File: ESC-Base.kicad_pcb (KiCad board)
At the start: 2 copper layers, 32 x 51.8 mm, 35 parts, among them P1 CONN_01X03, P2 CONN_01X05, P3 CONN_01X05, P4 CONN_01X02, P5 CONN_01X02, P6 CONN_01X04, P7 CONN_01X04, P8 CONN_01X02, U1 LM1084IS-5.0/NOPB, U2 VND5E006ASPTR, U3 LTV-817, U4 ACS712_30A, U5 ACS712_30A, U6 LTV-817, U7 LTV-817

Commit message: Weiter gearbeitet...
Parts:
- C4, D1, R1, R3, R5, R6, R7, R9, U1: moved to B.Cu
- U3: footprint sven:LTV817-Footprint -> toni:SO-4
- U6, U7: footprint sven:LTV817-Footprint -> toni:SO-4; moved to B.Cu
- moved C4 126.5 mm to (59.8, 90.0), turned to 180 degrees
- moved R8 123.7 mm to (57.0, 119.0), turned to 90 degrees
- moved R7 115.9 mm to (55.4, 106.4), turned to 90 degrees
- moved R10 112.9 mm to (71.9, 119.3), turned to 90 degrees
- moved C3 108.1 mm to (48.5, 102.4), turned to 180 degrees
- moved C1 104.9 mm to (48.5, 99.5), turned to 180 degrees
- moved R9 104.4 mm to (73.7, 104.4), turned to 90 degrees
- moved R1 100.1 mm to (58.6, 92.2)
- moved C2 94.7 mm to (48.5, 97.3), turned to 180 degrees
- moved U7 92.3 mm to (73.4, 111.4), turned to 0 degrees
- moved C8 89.9 mm to (58.8, 111.6), turned to 90 degrees
- moved R3 87.9 mm to (66.3, 91.2), turned to 270 degrees
- moved C6 87.7 mm to (61.0, 109.8), turned to 90 degrees
- moved R6 85.3 mm to (68.6, 91.2), turned to 270 degrees
- moved R5 77.2 mm to (70.3, 91.2), turned to 270 degrees
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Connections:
- R7 pad 2: Net-(P4-Pad2) -> /OUT2
- R9 pad 2: Net-(P5-Pad2) -> /OUT1
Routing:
- net GND: track 0.00 -> 210.4 mm, vias 0 -> 2
- net /OUT2: track 0.00 -> 56.3 mm, vias 0 -> 20
- net VCC: track 0.00 -> 39.2 mm, vias 0 -> 10
- net /OUT1: track 0.00 -> 38.5 mm, vias 0 -> 13
- net +5V: track 3.27 -> 31.9 mm, vias 0 -> 2
- net /Vcheck2: track 0.00 -> 27.1 mm, vias 0 -> 1
- net /Vcheck1: track 0.00 -> 25.2 mm, vias 0 -> 1
- net Net-(P3-Pad3): track 0.00 -> 24.5 mm, vias 0 -> 2
- net /GNDcheck2: track 0.00 -> 21.6 mm
- net /GNDcheck1: track 0.00 -> 19.7 mm
- net Net-(P2-Pad3): track 0.00 -> 19.2 mm
- net Net-(P4-Pad2): track 0.00 -> 16.1 mm
- net Net-(P3-Pad5): track 0.00 -> 13.2 mm, vias 0 -> 1
- net Net-(C1-Pad1): track 0.00 -> 12.0 mm, vias 0 -> 1
- net Net-(P2-Pad5): track 0.00 -> 11.8 mm, vias 0 -> 1
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- added copper zone on B.Cu, net /OUT1
- added copper zone on F.Cu, net /OUT1
- added copper zone on B.Cu, net /OUT2
- added copper zone on F.Cu, net /OUT2
- added copper zone on F.Cu, net GND
- added copper zone on F.Cu, net Net-(P4-Pad2)
- added copper zone on F.Cu, net Net-(P5-Pad2)
- added copper zone on B.Cu, net VCC
- added copper zone on F.Cu, net VCC
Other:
- net class 5V added: clearance 0.4, trace_width 0.25, via_dia 0.6, via_drill 0.4

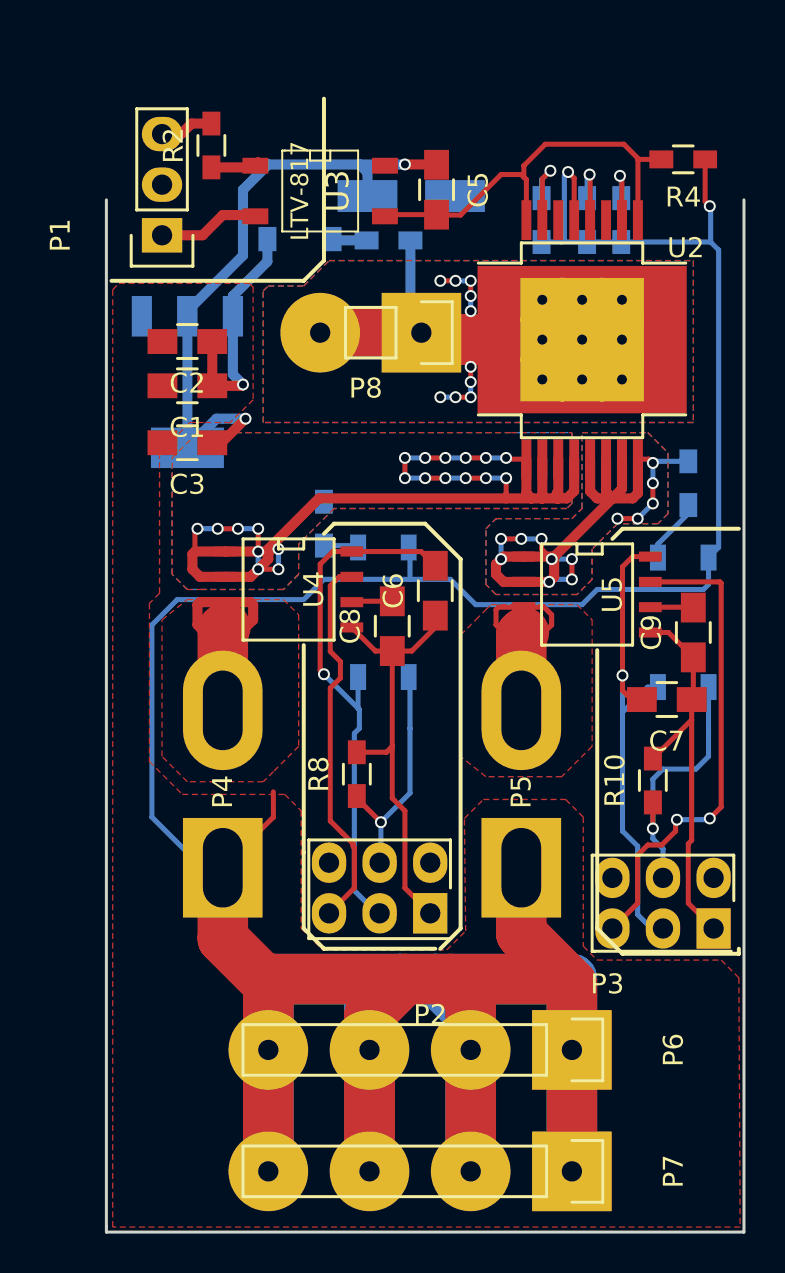
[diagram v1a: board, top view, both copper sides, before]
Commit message: Kleinere Optimierung+Netlist-Fix
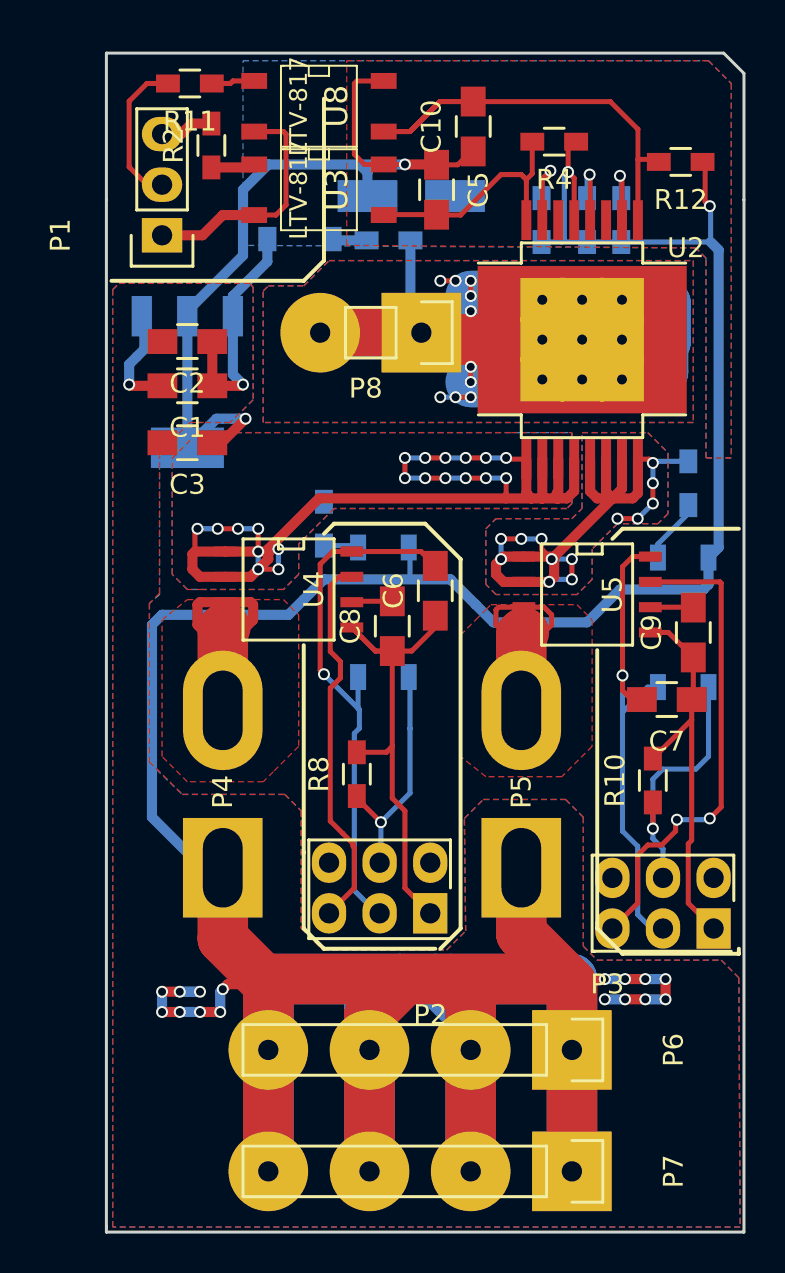
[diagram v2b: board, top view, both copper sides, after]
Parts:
- added C10: 100n, Capacitors_SMD:C_0805_HandSoldering, F.Cu at (62.9, 86.5)
- added R11: 1k, Resistors_SMD:R_0603_HandSoldering, F.Cu at (48.6, 84.3)
- added R12: 10k, Resistors_SMD:R_0603_HandSoldering, F.Cu at (73.3, 88.3)
- added U8: LTV-817, toni:SO-4, F.Cu at (55.1, 85.5)
- moved R4 6.54 mm to (66.9, 87.2)
- moved U3 0.09 mm to (55.1, 89.7)
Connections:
- U2 pad 9: /IN1 -> /IN2
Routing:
- net GND: track 210.4 -> 274.0 mm, vias 2 -> 19
- net VCC: track 39.2 -> 68.7 mm
- net /IN2: track 0.00 -> 24.8 mm
- net +5V: track 31.9 -> 41.8 mm
- net /IN1: track 21.4 -> 12.2 mm
- net Net-(P1-Pad2): track 0.00 -> 7.64 mm
- net Net-(P1-Pad1): track 9.73 -> 16.8 mm
- net /GNDcheck2: track 21.6 -> 24.7 mm
- net Net-(R11-Pad1): track 0.00 -> 2.18 mm
- added copper zone on B.Cu, net GND
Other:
- board size 32 x 51.8 mm -> 32 x 59.2 mm
- board text added: "ESC connector"
- board text added: "Sven T. S."

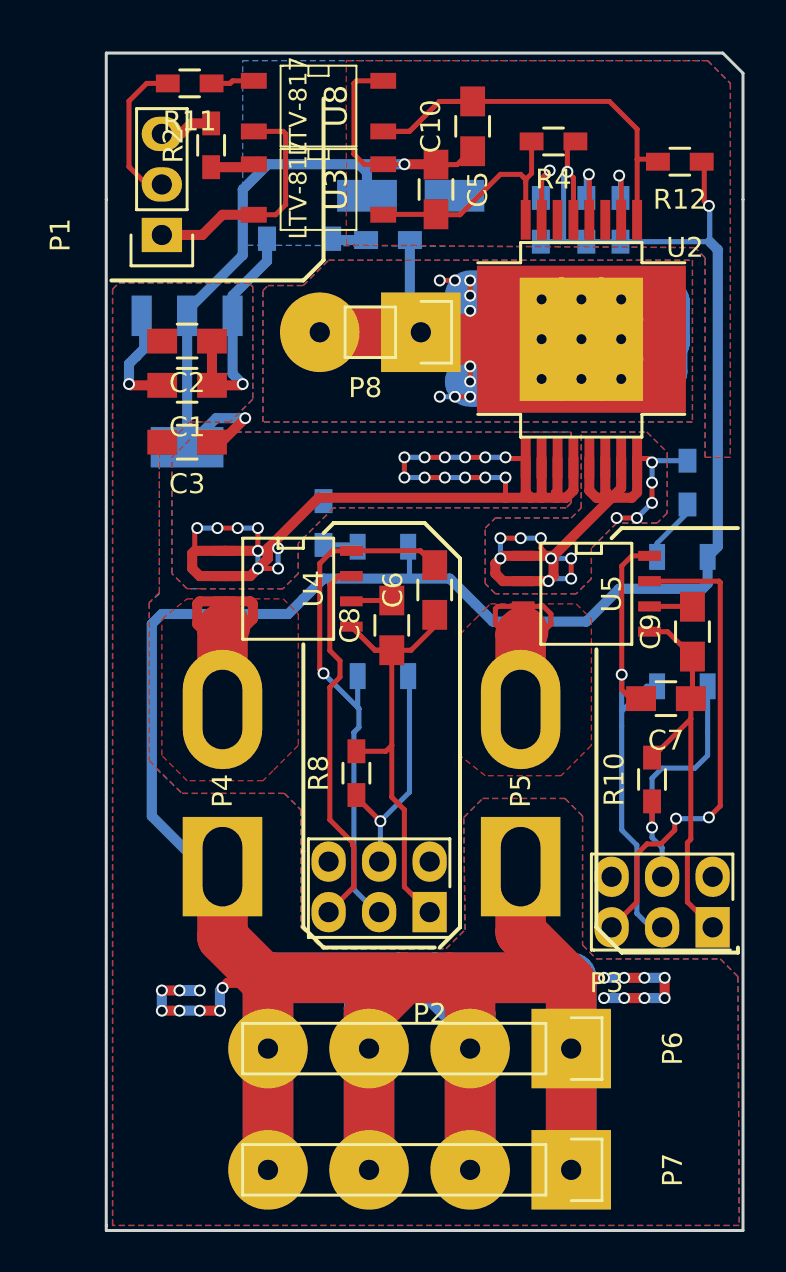
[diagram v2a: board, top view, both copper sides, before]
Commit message: Bohrungen, Lötstopplack und Bestückungsdruck: Alles Fertig!
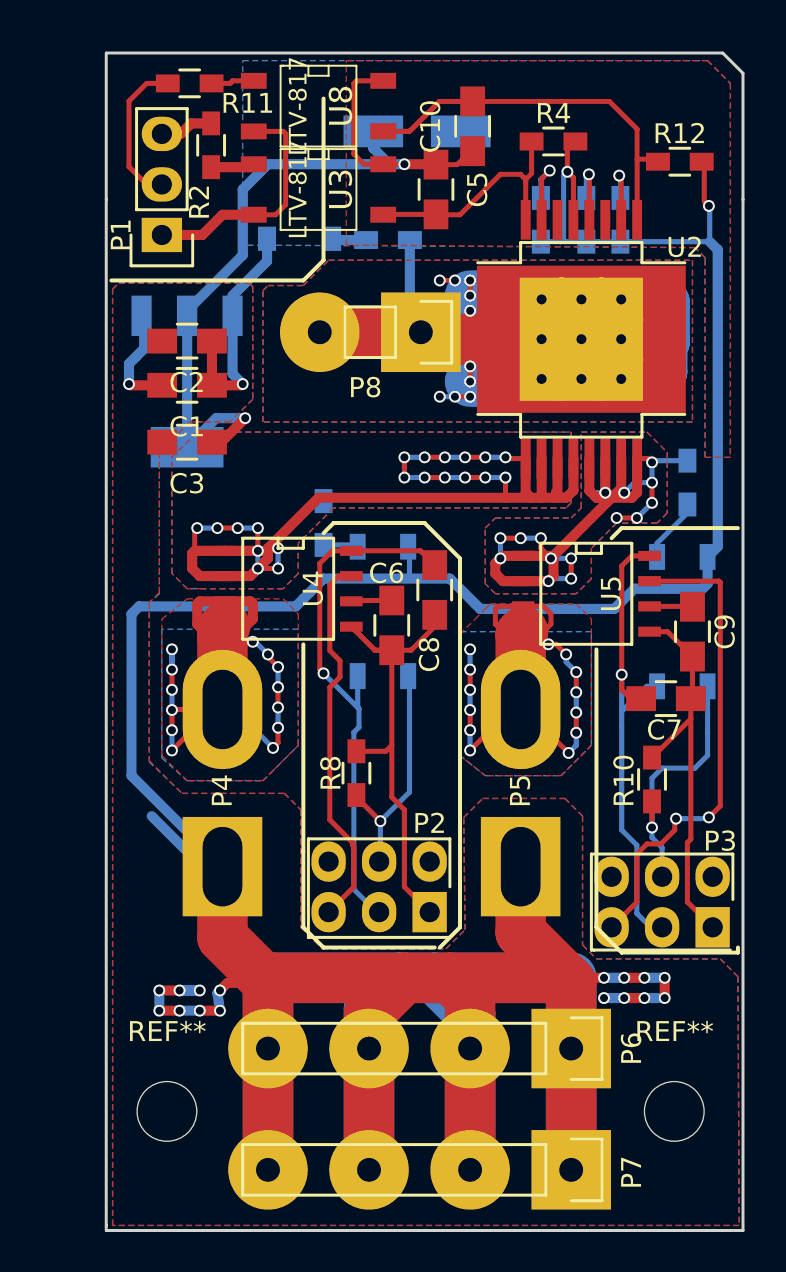
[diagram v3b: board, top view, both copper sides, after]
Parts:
- added REF**: MountingHole_3mm, Mounting_Holes:MountingHole_3mm, F.Cu at (47.5, 136.0)
- added REF**: MountingHole_3mm, Mounting_Holes:MountingHole_3mm, F.Cu at (73.0, 136.0)
- U1: value LM1084IS-5.0/NOPB -> LM1084IS-5.0
- moved C4 3.25 mm to (60.1, 86.7)
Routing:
- net Net-(P4-Pad2): track 16.1 -> 39.1 mm, vias 0 -> 13
- net Net-(P5-Pad2): track 11.3 -> 29.6 mm, vias 0 -> 13
- net GND: track 274.0 -> 269.9 mm
- net /OUT1: track 38.5 -> 41.9 mm, vias 13 -> 15
- net +5V: track 41.8 -> 43.2 mm
- added copper zone on B.Cu, net Net-(P4-Pad2)
- added copper zone on B.Cu, net Net-(P5-Pad2)
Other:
- rule pad_to_mask_clearance: 0.2 -> 0.1
